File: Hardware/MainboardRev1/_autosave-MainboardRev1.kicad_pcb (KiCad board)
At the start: 4 copper layers, 92 x 92 mm, 210 parts, among them J1 BACKUP_BATT: 1586038-2, J10 Switch_3, J11 Switch_2, J12 Switch_4, J13 EXTRA_5V, J14 EXTRA_3V3, J2 MAIN_BATT: 1586038-2, J3 Servo_Control, J4 EMATCH_1: 1586038-2, J5 EMATCH_2: 1586038-2, J6 Stratologger_PWR: 1586038-2, J7 Stratologger_DATA, J8 0733910320 [915MHz SMA], J9 Switch_1, Q1 SSM3J328R, Q10 SSM3J328R, Q11 NTR4003, Q12 NTR4003, Q13 NTR4003, Q14 SSM3J328R, Q15 NTR4003, Q16 SSM3J328R, Q17 SSM3J328R, Q18 NTR4003, Q19 NTR4003, Q2 SSM3J328R, Q20 SIS612EDNT-T1-GE3, Q21 SIS612EDNT-T1-GE3, Q22 NTR4003, Q23 NTR4003, Q24 NTR4003, Q25 SSM3J328R, Q26 NTR4003, Q3 SSM3J328R, Q4 SSM3J328R, Q5 NTR4003, Q6 NTR4003, Q7 NTR4003, Q8 SSM3J328R, Q9 NTR4003, SW1 EG2201A [DPDT], U1 LT6703-3, U10 LTC4358, U11 Teensy3.6, U12 ABPMANN030PG2A3, U13 LSM9DS1, U14 LIS331HH, U15 BME280, U16 CCS811, U17 ublox_max-m8q, U18 RFM69HCW, U2 LTC3605, U3 LTC4358, U4 LTC4358, U5 LDL1117S50R, U6 LDL1117S33R, U7 LTC2992, U8 LDL1117S33R, U9 LTC2992

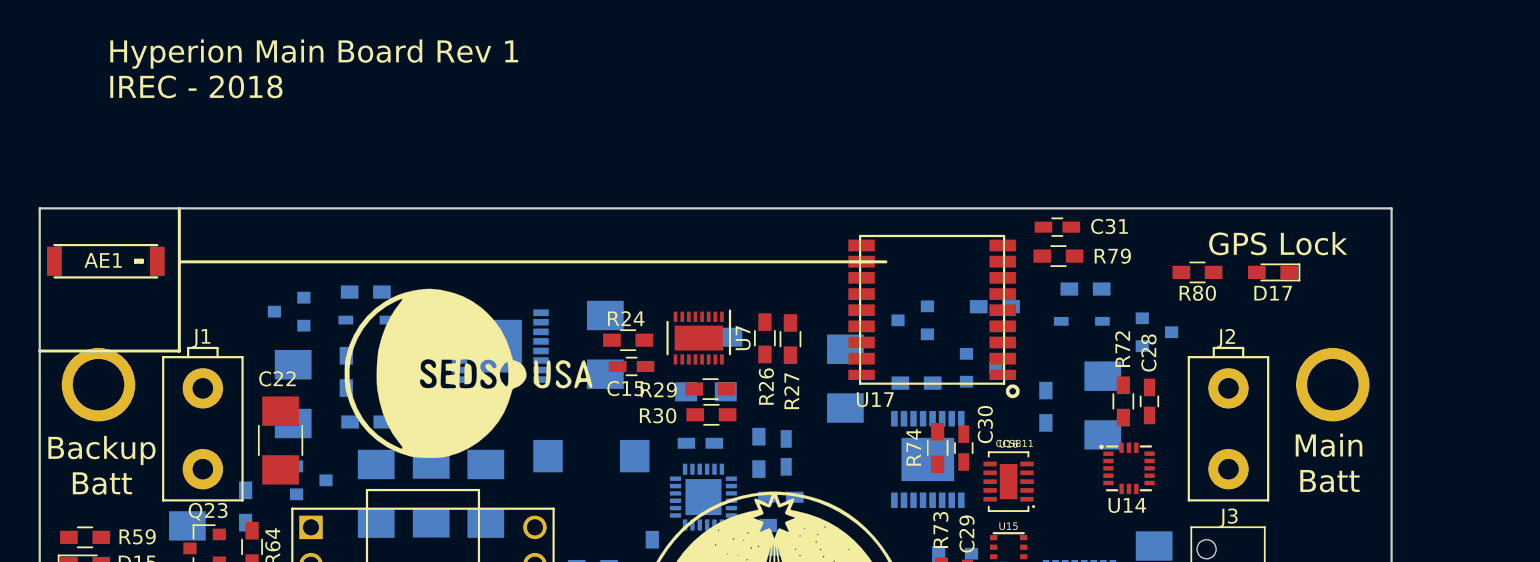
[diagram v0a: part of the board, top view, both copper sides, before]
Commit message: Added to silkscreen. Updated schematic pdf
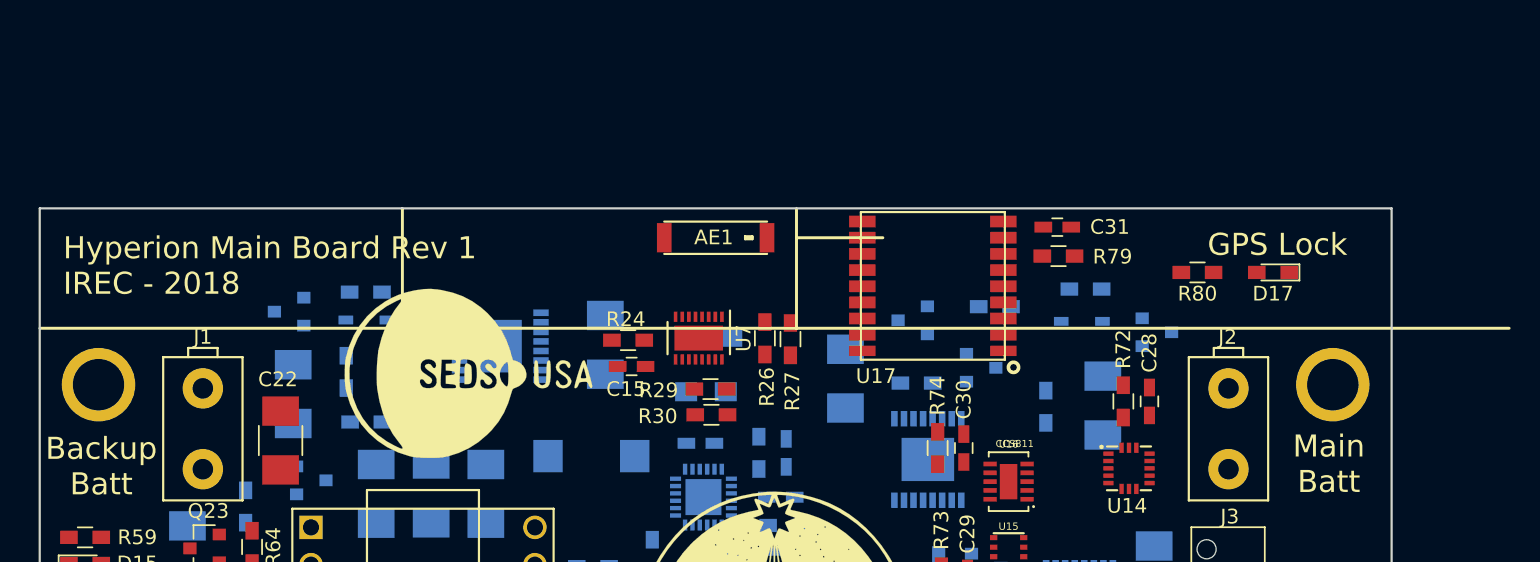
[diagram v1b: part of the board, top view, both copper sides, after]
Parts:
- moved AE1 41.5 mm to (96.0, 52.0)
- moved U17 1.63 mm to (110.8, 59.7)
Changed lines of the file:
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@@
     (area 49.924999 49.924999 142.075001 142.075001)
     (thickness 1.6)
-    (drawings 36)
+    (drawings 38)
     (tracks 0)
     (zones 0)
@@
     (46 B.CrtYd user)
     (47 F.CrtYd user)
-    (48 B.Fab user hide)
-    (49 F.Fab user hide)
+    (48 B.Fab user)
+    (49 F.Fab user)
   )
   (setup
@@
     (tags "capacitor 0603")
     (attr smd)
-    (fp_text reference C30 (at 1.602 1.504 90) (layer F.SilkS)
+    (fp_text reference C30 (at 3.302 0 90) (layer F.SilkS)
       (effects (font (size 1 1) (thickness 0.15)))
     )
@@
     (tags "resistor 0603")
     (attr smd)
-    (fp_text reference R74 (at 0.012 -1.588 90) (layer F.SilkS)
+    (fp_text reference R74 (at 3.556 0 90) (layer F.SilkS)
       (effects (font (size 1 1) (thickness 0.15)))
     )
@@
       (net 4 GND))
   )
-  (module _sensors:MAX-M8 (layer F.Cu)
-    (at 110.73 61.33 180)
+  (module _sensors:MAX-M8 locked (layer F.Cu)
+    (at 110.78 59.7 180)
     (fp_text reference U17 (at 3.87 -1.72 180) (layer F.SilkS)
       (effects (font (size 1 1) (thickness 0.15)))
@@
   )
   (module Dans_Parts:ANT_CHIP_OMNI_1575MHz_GPS locked (layer F.Cu)
-    (at 54.5 53.6)
+    (at 96 52)
     (fp_text reference AE1 (at -0.13 -0.02) (layer F.SilkS)
       (effects (font (size 1 1) (thickness 0.15)))
@@
       (xy -0.015338 -0.672556)) (layer F.SilkS) (width 0.01))
   )
-  (gr_line (start 59.51 53.64) (end 107.59 53.64) (angle 90) (layer F.SilkS) (width 0.2))
-  (gr_line (start 59.5 50) (end 59.5 59.73) (angle 90) (layer F.SilkS) (width 0.2))
-  (gr_line (start 49.98 59.71) (end 59.5 59.71) (angle 90) (layer F.SilkS) (width 0.2))
+  (gr_line (start 74.68 50.03) (end 74.66 50.03) (angle 90) (layer F.SilkS) (width 0.2))
+  (gr_line (start 74.68 58.29) (end 74.68 50.03) (angle 90) (layer F.SilkS) (width 0.2))
+  (gr_line (start 101.5 52) (end 107.38 52) (angle 90) (layer F.SilkS) (width 0.2))
+  (gr_line (start 101.5 50) (end 101.5 58.16) (angle 90) (layer F.SilkS) (width 0.2))
+  (gr_line (start 150 58.16) (end 50 58.16) (angle 90) (layer F.SilkS) (width 0.2))
   (gr_text "Tigris\nAd Astra" (at 91.53 89.86) (layer F.SilkS)
     (effects (font (size 1.5 1.5) (thickness 0.3)))
@@
     (effects (font (size 1.5 1.5) (thickness 0.3)))
   )
-  (gr_text "Hyperion Main Board Rev 1\nIREC - 2018" (at 54.6 40.58) (layer F.SilkS)
+  (gr_text "Hyperion Main Board Rev 1\nIREC - 2018" (at 51.59 53.91) (layer F.SilkS)
     (effects (font (size 1.5 1.5) (thickness 0.3)) (justify left))
   )
